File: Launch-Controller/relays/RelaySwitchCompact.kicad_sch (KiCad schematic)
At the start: 13 parts, among them J1 Conn_01x05_Pin, K1 1-1721150-0, U1 FOD817ASD, U2 FMMT634QTA

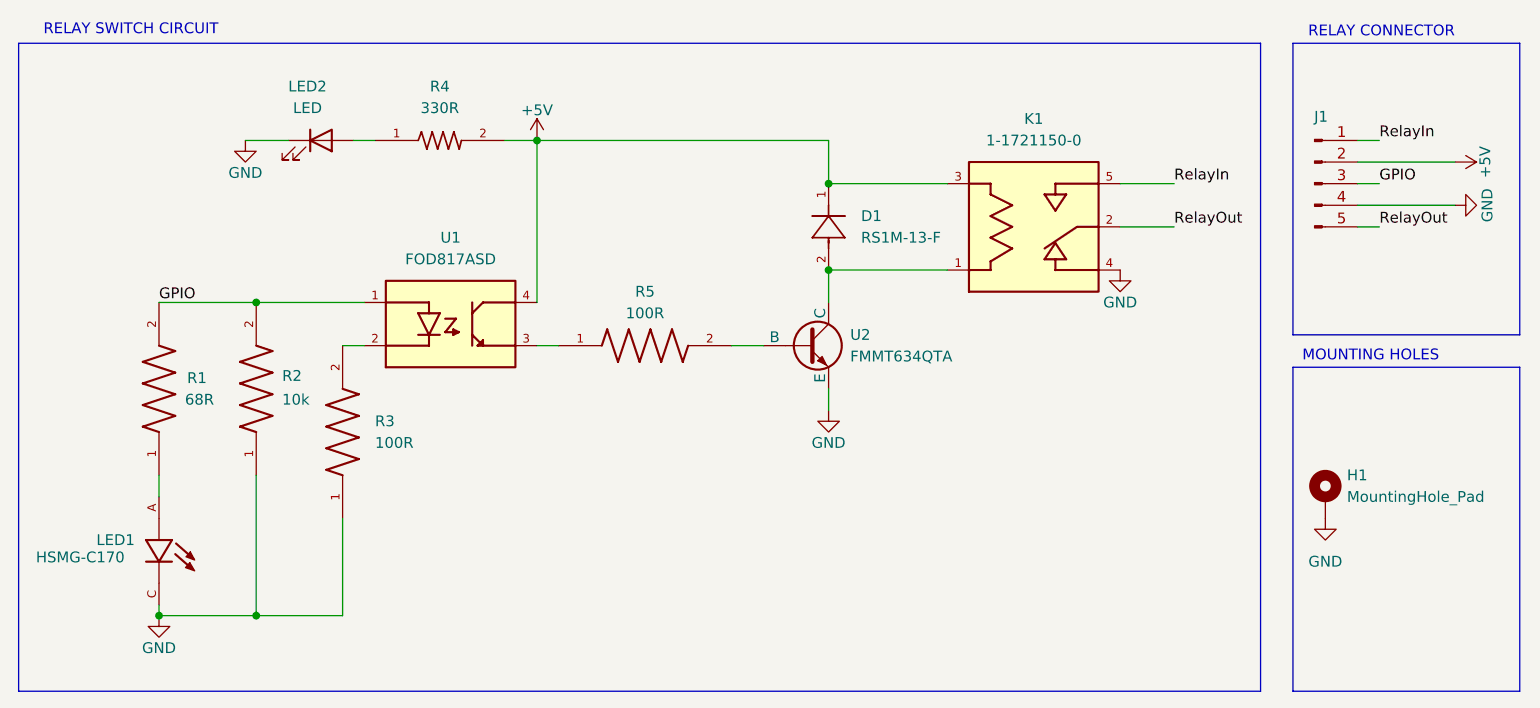
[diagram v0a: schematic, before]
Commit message: fized relay
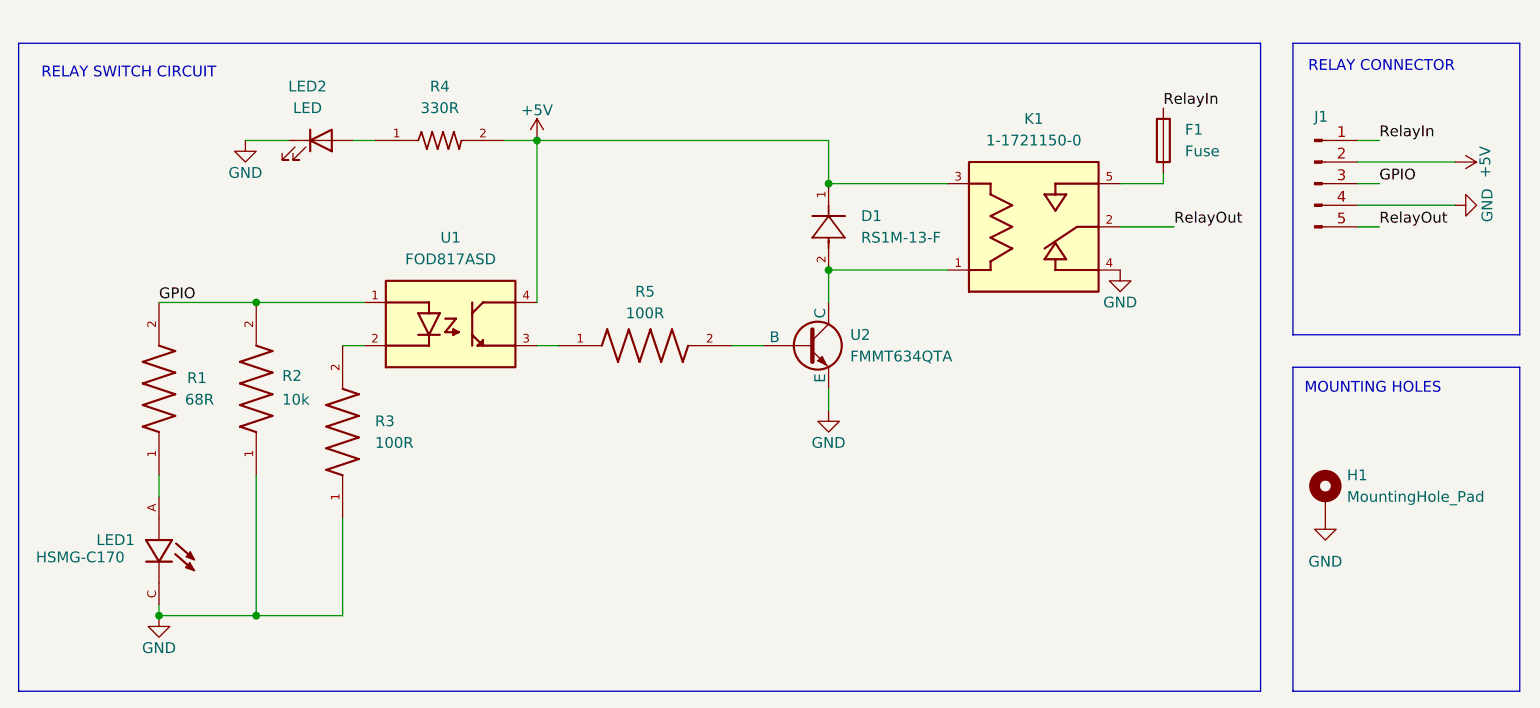
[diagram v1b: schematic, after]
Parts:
- added F1: Fuse, Diode_SMD:D_0402_1005Metric_Pad0.77x0.64mm_HandSolder, symbol Device:Fuse
- R1: footprint CRCW0402140RFKEDC:RESC1005X35N -> Resistor_SMD:R_0402_1005Metric_Pad0.72x0.64mm_HandSolder
- R2: footprint CRCW060310K0DHEAP:RESC1508X50N -> Resistor_SMD:R_0603_1608Metric_Pad0.98x0.95mm_HandSolder
- R3, R5: footprint AC0603JR-07100RL:RESC1608X55N -> Resistor_SMD:R_0603_1608Metric_Pad0.98x0.95mm_HandSolder
- R4: footprint RC0603FR-07330RL:RESC1607X60N -> Resistor_SMD:R_0603_1608Metric_Pad0.98x0.95mm_HandSolder
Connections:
- net RelayIn: now also F1.1; no longer K1.5
- new net: F1.2, K1.5
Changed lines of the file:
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@@
+	(wire
+		(pts
+			(xy 147.32 36.83) (xy 152.4 36.83)
+		)
+		(stroke
+			(width 0)
+			(type default)
+		)
+	)
 	(wire
 		(pts
@@
 	(wire
 		(pts
-			(xy 147.32 36.83) (xy 153.67 36.83)
+			(xy 152.4 36.83) (xy 152.4 35.56)
 		)
 		(stroke
@@
 	(text "MOUNTING HOLES"
 		(exclude_from_sim no)
-		(at 176.784 57.15 0)
+		(at 177.038 60.96 0)
 		(effects
 			(font
@@
 	(text "RELAY CONNECTOR"
 		(exclude_from_sim no)
-		(at 178.054 19.05 0)
+		(at 178.054 23.114 0)
 		(effects
 			(font
@@
 	(text "RELAY SWITCH CIRCUIT"
 		(exclude_from_sim no)
-		(at 30.988 18.796 0)
+		(at 30.734 23.876 0)
 		(effects
 			(font
@@
 	)
 	(label "RelayIn"
-		(at 153.67 36.83 0)
+		(at 152.4 27.94 0)
 		(fields_autoplaced yes)
 		(effects
@@
 	)
 	(symbol
+		(lib_id "Device:Fuse")
+		(at 152.4 31.75 0)
+		(unit 1)
+		(exclude_from_sim no)
+		(in_bom yes)
+		(on_board yes)
+		(dnp no)
+		(fields_autoplaced yes)
+		(property "Reference" "F1"
+			(at 154.94 30.4799 0)
+			(effects
+				(font
+					(size 1.27 1.27)
+				)
+				(justify left)
+			)
+		)
+		(property "Value" "Fuse"
+			(at 154.94 33.0199 0)
+			(effects
+				(font
+					(size 1.27 1.27)
+				)
+				(justify left)
+			)
+		)
+		(property "Footprint" "Diode_SMD:D_0402_1005Metric_Pad0.77x0.64mm_HandSolder"
+			(at 150.622 31.75 90)
+			(effects
+				(font
+					(size 1.27 1.27)
+				)
+				(hide yes)
+			)
+		)
+		(property "Datasheet" "~"
+			(at 152.4 31.75 0)
+			(effects
+				(font
+					(size 1.27 1.27)
+				)
+				(hide yes)
+			)
+		)
+		(property "Description" "Fuse"
+			(at 152.4 31.75 0)
+			(effects
+				(font
+					(size 1.27 1.27)
+				)
+				(hide yes)
+			)
+		)
+		(pin "2"
+		)
+		(pin "1"
+		)
+		(instances
+			(project ""
+				(path "/17917494-3591-49e5-9749-7de8031f33d3"
+					(reference "F1")
+					(unit 1)
+				)
+			)
+		)
+	)
+	(symbol
 		(lib_id "CRCW060310K0DHEAP:CRCW060310K0DHEAP")
 		(at 45.72 60.96 90)
@@
 			)
 		)
-		(property "Footprint" "CRCW060310K0DHEAP:RESC1508X50N"
+		(property "Footprint" "Resistor_SMD:R_0603_1608Metric_Pad0.98x0.95mm_HandSolder"
 			(at 45.72 60.96 0)
 			(effects
@@
 			)
 		)
-		(property "Footprint" "RC0603FR-07330RL:RESC1607X60N"
+		(property "Footprint" "Resistor_SMD:R_0603_1608Metric_Pad0.98x0.95mm_HandSolder"
 			(at 67.31 31.75 0)
 			(effects
@@
 			)
 		)
-		(property "Footprint" "CRCW0402140RFKEDC:RESC1005X35N"
+		(property "Footprint" "Resistor_SMD:R_0402_1005Metric_Pad0.72x0.64mm_HandSolder"
 			(at 34.29 60.96 0)
 			(effects
@@
 			)
 		)
-		(property "Footprint" "AC0603JR-07100RL:RESC1608X55N"
+		(property "Footprint" "Resistor_SMD:R_0603_1608Metric_Pad0.98x0.95mm_HandSolder"
 			(at 55.88 66.04 0)
 			(effects
@@
 			)
 		)
-		(property "Footprint" "AC0603JR-07100RL:RESC1608X55N"
+		(property "Footprint" "Resistor_SMD:R_0603_1608Metric_Pad0.98x0.95mm_HandSolder"
 			(at 91.44 55.88 0)
 			(effects
